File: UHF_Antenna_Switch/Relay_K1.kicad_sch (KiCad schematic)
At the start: 5 parts, among them K3 HF3-51, Q2 2N7002

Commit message: Assign most footprints
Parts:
- R3, R4: footprint (none) -> Resistor_SMD:R_0603_1608Metric_Pad0.98x0.95mm_HandSolder
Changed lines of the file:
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@@
 			)
 		)
-		(property "Footprint" ""
+		(property "Footprint" "Resistor_SMD:R_0603_1608Metric_Pad0.98x0.95mm_HandSolder"
 			(at 84.582 110.49 90)
 			(hide yes)
@@
 			)
 		)
-		(property "Footprint" ""
+		(property "Footprint" "Resistor_SMD:R_0603_1608Metric_Pad0.98x0.95mm_HandSolder"
 			(at 80.01 103.378 90)
 			(hide yes)

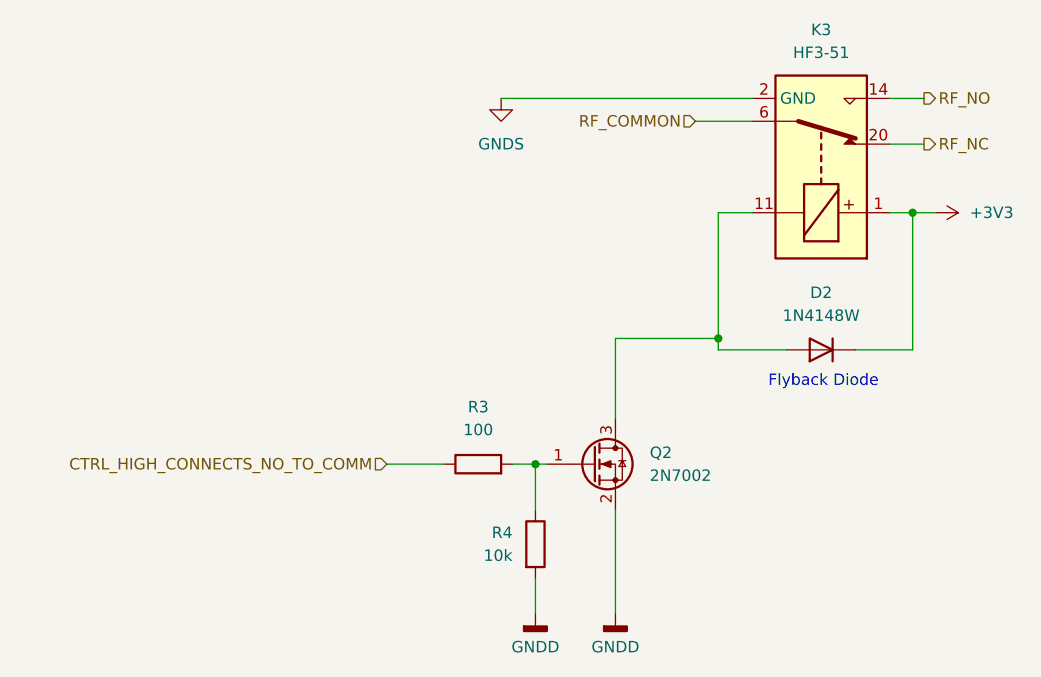
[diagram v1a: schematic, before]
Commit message: Add preliminary footprint to directional coupler and begin layout
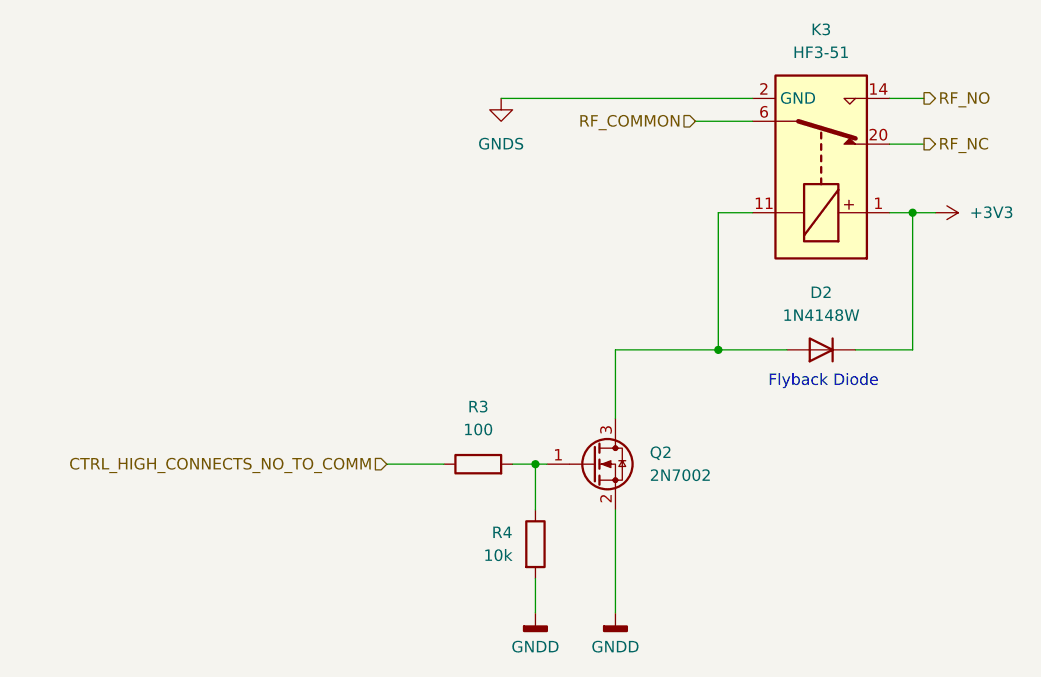
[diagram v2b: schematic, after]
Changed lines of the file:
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@@
 	)
 	(junction
-		(at 106.68 87.63)
+		(at 106.68 88.9)
 		(diameter 0)
 		(color 0 0 0 0)
@@
 	(wire
 		(pts
-			(xy 95.25 96.52) (xy 95.25 87.63)
+			(xy 95.25 96.52) (xy 95.25 88.9)
 		)
 		(stroke
@@
 	(wire
 		(pts
-			(xy 95.25 87.63) (xy 106.68 87.63)
+			(xy 95.25 88.9) (xy 106.68 88.9)
 		)
 		(stroke
@@
 	(wire
 		(pts
-			(xy 106.68 88.9) (xy 106.68 87.63)
+			(xy 106.68 73.66) (xy 106.68 88.9)
 		)
 		(stroke
-			(width 0)
-			(type default)
-		)
-	)
-	(wire
-		(pts
-			(xy 106.68 87.63) (xy 106.68 73.66)
-		)
-		(stroke

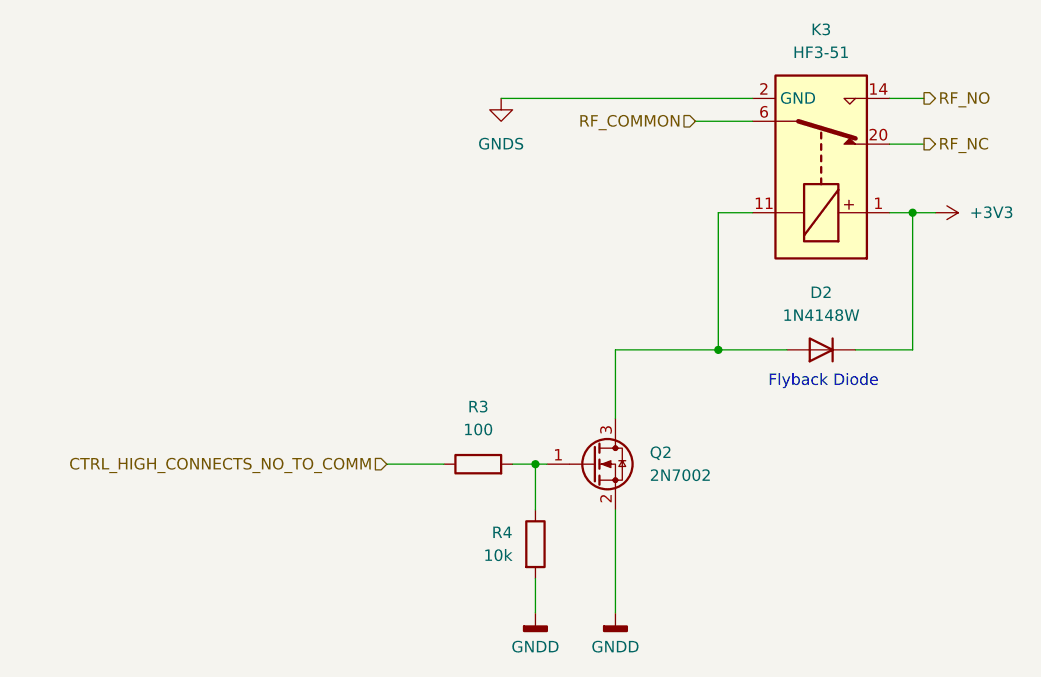
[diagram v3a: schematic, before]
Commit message: PCB: Route digital components
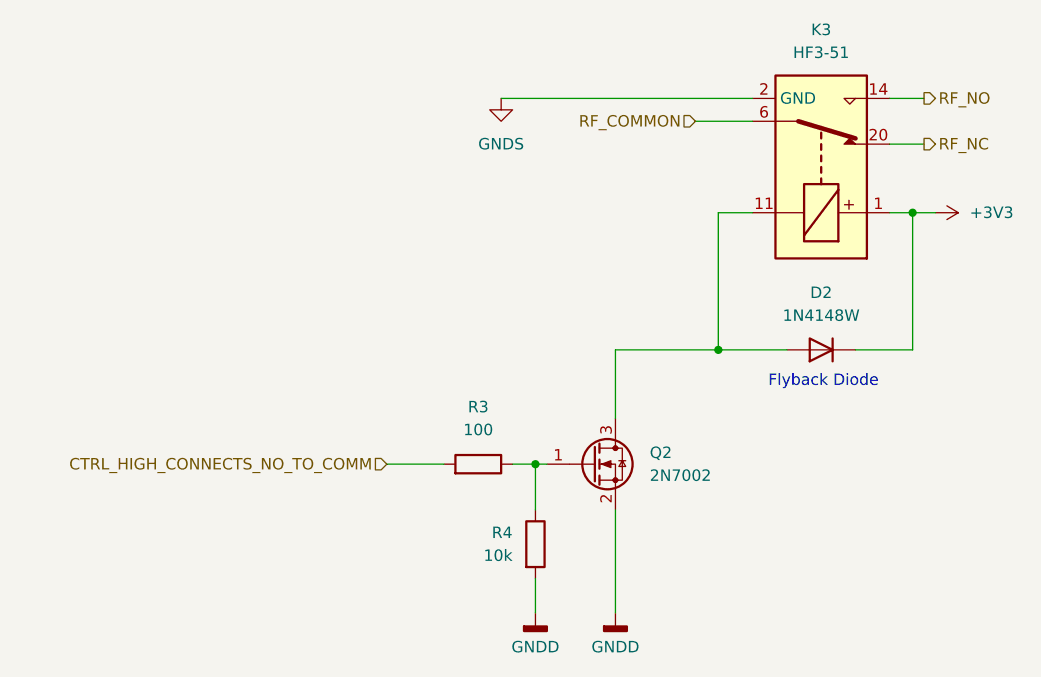
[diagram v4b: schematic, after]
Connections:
- net CTRL_HIGH_CONNECTS_NO_TO_COMM: now also R3.2; no longer R3.1
- net at Q2.1 (G), R4.1: now also R3.1; no longer R3.2
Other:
- moved on the sheet: R3
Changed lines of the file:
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@@
 	(symbol
 		(lib_id "Device:R")
-		(at 80.01 101.6 90)
+		(at 80.01 101.6 270)
+		(mirror x)
 		(unit 1)
 		(body_style 1)
@@
 		(in_pos_files yes)
 		(dnp no)
-		(fields_autoplaced yes)
 		(property "Reference" "R3"
 			(at 80.01 95.25 90)

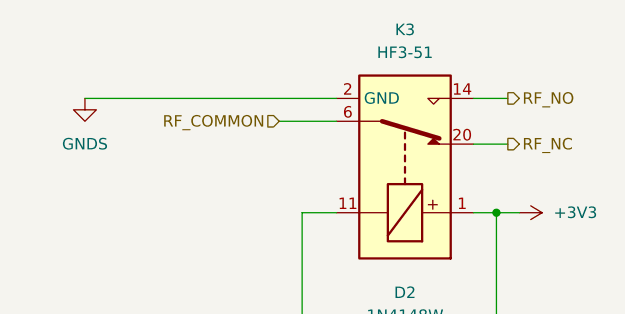
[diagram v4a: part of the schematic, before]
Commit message: PCB: Add many labels
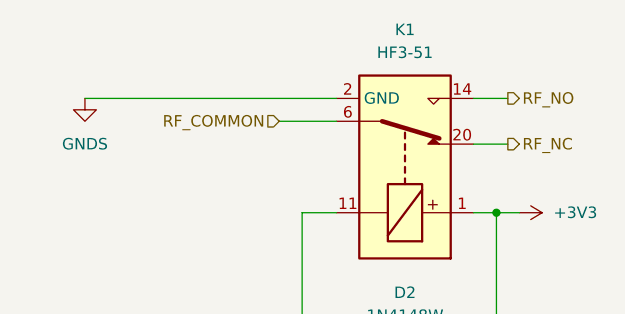
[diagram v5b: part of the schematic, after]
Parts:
- renumbered K3 to K1
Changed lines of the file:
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@@
 		(dnp no)
 		(fields_autoplaced yes)
-		(property "Reference" "K3"
+		(property "Reference" "K1"
 			(at 118.11 53.34 90)
 			(show_name no)
@@
 			(project "UHF_Antenna_Switch"
 				(path "/0ffb5503-f768-4a51-945c-501d4ddb5b7c/7c92ed6c-a81f-4de6-ac62-7d4cfa37592e"
-					(reference "K3")
+					(reference "K1")
 					(unit 1)
 				)
 				(path "/0ffb5503-f768-4a51-945c-501d4ddb5b7c/9d81a56d-3e74-45da-8801-f425c0b0835d"
-					(reference "K4")
+					(reference "K2")
 					(unit 1)
 				)
